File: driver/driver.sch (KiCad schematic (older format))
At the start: 104 parts, among them J1 OUT_A, J2 OUT_B, J3 UART_DEBUG, J4 USB_B_Micro, J5 CH340E module, J6 1602 I2C LCD, J7 IN_VCC, J8 IN_GND, J9 SWD, Q1 TPHR6503PL, Q2 TPHR6503PL, Q3 TPHR6503PL, Q4 TPHR6503PL, SW1 SW_Push, SW2 SW_Push, U1 MT3608, U10 PC817, U2 AMS1117-5.0, U3 AMS1117-3.3, U4 TC4427, U5 TC4427, U6 STM32F103C8Tx, U7 INA226, U8 MCP9804_MSOP, U9 PC817, Y1 8MHz

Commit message: Fix R1 footprint
0603 -> 1206
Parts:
- R1: footprint Resistor_SMD:R_0603_1608Metric_Pad1.05x0.95mm_HandSolder -> Resistor_SMD:R_1206_3216Metric_Pad1.42x1.75mm_HandSolder
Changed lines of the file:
@@
 F 0 "R1" V 12654 2050 50  0000 C CNN
 F 1 "10R .5W" V 12745 2050 50  0000 C CNN
-F 2 "Resistor_SMD:R_0603_1608Metric_Pad1.05x0.95mm_HandSolder" H 12850 2050 50  0001 C CNN
+F 2 "Resistor_SMD:R_1206_3216Metric_Pad1.42x1.75mm_HandSolder" H 12850 2050 50  0001 C CNN
 F 3 "~" H 12850 2050 50  0001 C CNN
 	1    12850 2050

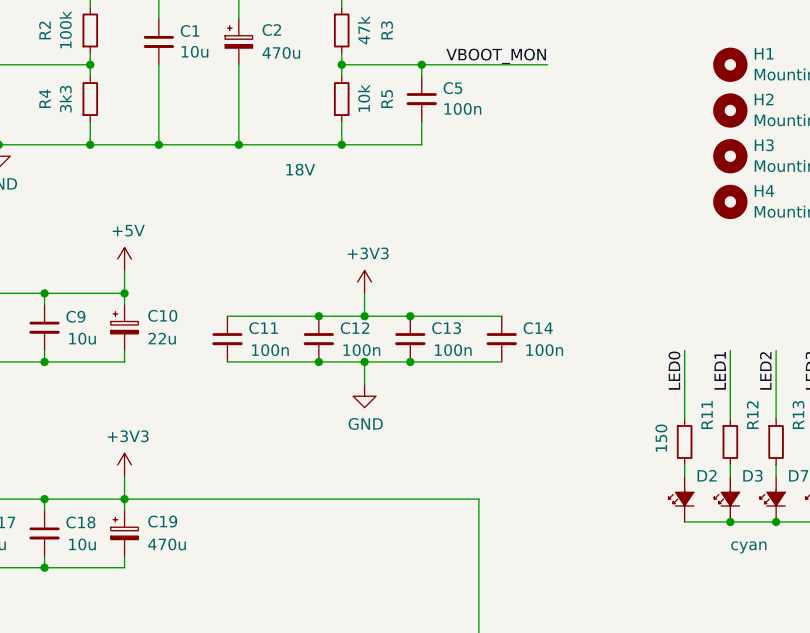
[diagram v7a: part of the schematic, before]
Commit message: Modify temp sensor to MSOP fp, add fan conn
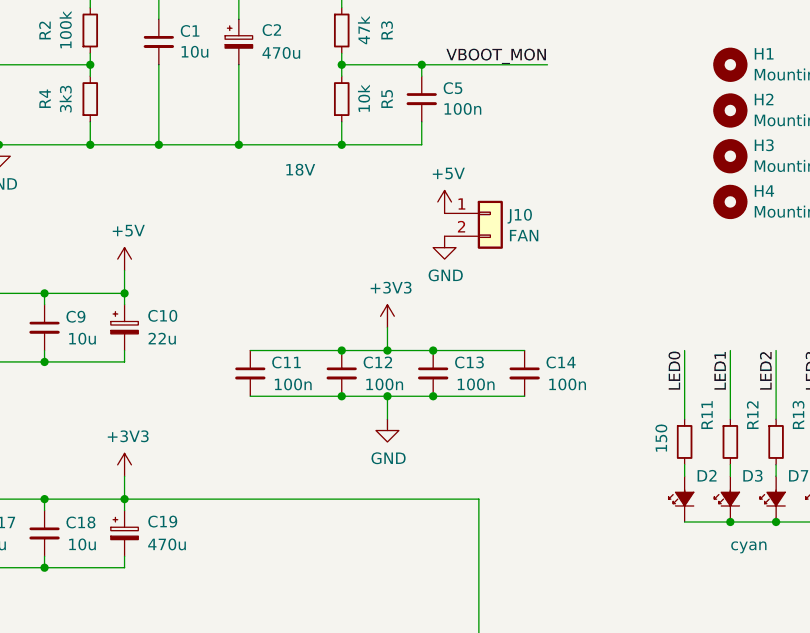
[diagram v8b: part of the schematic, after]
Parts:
- added J10: FAN, Connectors_Molex:Molex_KK-6410-02_02x2.54mm_Straight, symbol Connector_Generic:Conn_01x02
- U8: footprint Package_SO:SOIC-8_3.9x4.9mm_P1.27mm -> Package_SO:MSOP-8_3x3mm_P0.65mm
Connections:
- net +5V: now also J10.1 (Pin_1)
- net GND: now also J10.2 (Pin_2)
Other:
- moved on the sheet: C11, C12, C13, C14
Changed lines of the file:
@@
 L Device:C_Small C11
 U 1 1 5C5BBF20
-P 15550 3400
-F 0 "C11" H 15642 3446 50  0000 L CNN
-F 1 "100n" H 15650 3350 50  0000 L CNN
-F 2 "Capacitors_SMD:C_0603_HandSoldering" H 15550 3400 50  0001 C CNN
-F 3 "~" H 15550 3400 50  0001 C CNN
-	1    15550 3400
+P 15650 3550
+F 0 "C11" H 15742 3596 50  0000 L CNN
+F 1 "100n" H 15750 3500 50  0000 L CNN
+F 2 "Capacitors_SMD:C_0603_HandSoldering" H 15650 3550 50  0001 C CNN
+F 3 "~" H 15650 3550 50  0001 C CNN
+	1    15650 3550
 	1    0    0    -1
 $EndComp
@@
 L Device:C_Small C12
 U 1 1 5C5BD76D
-P 15950 3400
-F 0 "C12" H 16042 3446 50  0000 L CNN
-F 1 "100n" H 16050 3350 50  0000 L CNN
-F 2 "Capacitors_SMD:C_0603_HandSoldering" H 15950 3400 50  0001 C CNN
-F 3 "~" H 15950 3400 50  0001 C CNN
-	1    15950 3400
+P 16050 3550
+F 0 "C12" H 16142 3596 50  0000 L CNN
+F 1 "100n" H 16150 3500 50  0000 L CNN
+F 2 "Capacitors_SMD:C_0603_HandSoldering" H 16050 3550 50  0001 C CNN
+F 3 "~" H 16050 3550 50  0001 C CNN
+	1    16050 3550
 	1    0    0    -1
 $EndComp
@@
 L Device:C_Small C13
 U 1 1 5C5C8D7A
-P 16350 3400
-F 0 "C13" H 16442 3446 50  0000 L CNN
-F 1 "100n" H 16450 3350 50  0000 L CNN
-F 2 "Capacitors_SMD:C_0603_HandSoldering" H 16350 3400 50  0001 C CNN
-F 3 "~" H 16350 3400 50  0001 C CNN
-	1    16350 3400
+P 16450 3550
+F 0 "C13" H 16542 3596 50  0000 L CNN
+F 1 "100n" H 16550 3500 50  0000 L CNN
+F 2 "Capacitors_SMD:C_0603_HandSoldering" H 16450 3550 50  0001 C CNN
+F 3 "~" H 16450 3550 50  0001 C CNN
+	1    16450 3550
 	1    0    0    -1
 $EndComp
@@
 L Device:C_Small C14
 U 1 1 5C5C9980
-P 16750 3400
-F 0 "C14" H 16842 3446 50  0000 L CNN
-F 1 "100n" H 16850 3350 50  0000 L CNN
-F 2 "Capacitors_SMD:C_0603_HandSoldering" H 16750 3400 50  0001 C CNN
-F 3 "~" H 16750 3400 50  0001 C CNN
-	1    16750 3400
+P 16850 3550
+F 0 "C14" H 16942 3596 50  0000 L CNN
+F 1 "100n" H 16950 3500 50  0000 L CNN
+F 2 "Capacitors_SMD:C_0603_HandSoldering" H 16850 3550 50  0001 C CNN
+F 3 "~" H 16850 3550 50  0001 C CNN
+	1    16850 3550
 	1    0    0    -1
 $EndComp
@@
 L power:+3V3 #PWR0117
 U 1 1 5C5CB59E
-P 16150 3200
-F 0 "#PWR0117" H 16150 3050 50  0001 C CNN
-F 1 "+3V3" H 16165 3373 50  0000 C CNN
-F 2 "" H 16150 3200 50  0001 C CNN
-F 3 "" H 16150 3200 50  0001 C CNN
-	1    16150 3200
-	1    0    0    -1
-$EndComp
-Wire Wire Line
-	15550 3300 15950 3300
-Connection ~ 15950 3300
-Wire Wire Line
-	15950 3300 16150 3300
-Connection ~ 16350 3300
-Wire Wire Line
-	16350 3300 16750 3300
-Wire Wire Line
-	16150 3200 16150 3300
-Connection ~ 16150 3300
-Wire Wire Line
-	16150 3300 16350 3300
+P 16250 3350
+F 0 "#PWR0117" H 16250 3200 50  0001 C CNN
+F 1 "+3V3" H 16265 3523 50  0000 C CNN
+F 2 "" H 16250 3350 50  0001 C CNN
+F 3 "" H 16250 3350 50  0001 C CNN
+	1    16250 3350
+	1    0    0    -1
+$EndComp
+Wire Wire Line
+	15650 3450 16050 3450
+Connection ~ 16050 3450
+Wire Wire Line
+	16050 3450 16250 3450
+Connection ~ 16450 3450
+Wire Wire Line
+	16450 3450 16850 3450
+Wire Wire Line
+	16250 3350 16250 3450
+Connection ~ 16250 3450
+Wire Wire Line
+	16250 3450 16450 3450
 $Comp
 L power:GND #PWR0118
 U 1 1 5C5DEABD
-P 16150 3600
-F 0 "#PWR0118" H 16150 3350 50  0001 C CNN
-F 1 "GND" H 16155 3427 50  0000 C CNN
-F 2 "" H 16150 3600 50  0001 C CNN
-F 3 "" H 16150 3600 50  0001 C CNN
-	1    16150 3600
-	1    0    0    -1
-$EndComp
-Wire Wire Line
-	15550 3500 15950 3500
-Connection ~ 15950 3500
-Wire Wire Line
-	15950 3500 16150 3500
-Connection ~ 16350 3500
-Wire Wire Line
-	16350 3500 16750 3500
-Wire Wire Line
-	16150 3500 16150 3600
-Connection ~ 16150 3500
-Wire Wire Line
-	16150 3500 16350 3500
+P 16250 3750
+F 0 "#PWR0118" H 16250 3500 50  0001 C CNN
+F 1 "GND" H 16255 3577 50  0000 C CNN
+F 2 "" H 16250 3750 50  0001 C CNN
+F 3 "" H 16250 3750 50  0001 C CNN
+	1    16250 3750
+	1    0    0    -1
+$EndComp
+Wire Wire Line
+	15650 3650 16050 3650
+Connection ~ 16050 3650
+Wire Wire Line
+	16050 3650 16250 3650
+Connection ~ 16450 3650
+Wire Wire Line
+	16450 3650 16850 3650
+Wire Wire Line
+	16250 3650 16250 3750
+Connection ~ 16250 3650
+Wire Wire Line
+	16250 3650 16450 3650
 $Comp
 L Device:C_Small C29
@@
 F 0 "U8" H 13250 8800 50  0000 L CNN
 F 1 "MCP9804_MSOP" V 13950 8450 50  0000 L CNN
-F 2 "Package_SO:SOIC-8_3.9x4.9mm_P1.27mm" H 12550 7850 50  0001 C CNN
+F 2 "Package_SO:MSOP-8_3x3mm_P0.65mm" H 12550 7850 50  0001 C CNN
 F 3 "http://ww1.microchip.com/downloads/en/DeviceDoc/22203b.pdf" H 13300 8800 50  0001 C CNN
 	1    13550 8350
@@
 Wire Wire Line
 	10150 6300 10150 6600
+$Comp
+L Connector_Generic:Conn_01x02 J10
+U 1 1 5C533914
+P 16700 2850
+F 0 "J10" H 16779 2842 50  0000 L CNN
+F 1 "FAN" H 16779 2751 50  0000 L CNN
+F 2 "Connectors_Molex:Molex_KK-6410-02_02x2.54mm_Straight" H 16700 2850 50  0001 C CNN
+F 3 "~" H 16700 2850 50  0001 C CNN
+	1    16700 2850
+	1    0    0    -1
+$EndComp
+$Comp
+L power:GND #PWR0147
+U 1 1 5C55EA3D
+P 16500 2950
+F 0 "#PWR0147" H 16500 2700 50  0001 C CNN
+F 1 "GND" H 16505 2777 50  0000 C CNN
+F 2 "" H 16500 2950 50  0001 C CNN
+F 3 "" H 16500 2950 50  0001 C CNN
+	1    16500 2950
+	1    0    0    -1
+$EndComp
+$Comp
+L power:+5V #PWR0148
+U 1 1 5C560259
+P 16500 2850
+F 0 "#PWR0148" H 16500 2700 50  0001 C CNN
+F 1 "+5V" H 16515 3023 50  0000 C CNN
+F 2 "" H 16500 2850 50  0001 C CNN
+F 3 "" H 16500 2850 50  0001 C CNN
+	1    16500 2850
+	1    0    0    -1
+$EndComp
 $EndSCHEMATC
